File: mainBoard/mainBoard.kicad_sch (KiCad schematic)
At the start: 51 parts, among them J1 XT60PW-M, J10 XT30U_F, J11 XT30U_F, J2 XT60PW-M, J3 XT30PW-M, J4 XT30PW-M, J5 Barrel_Jack, J6 XT30U_F, J7 XT30U_F, J8 XT30U_F, J9 XT30U_F, Q1 FQD11P06TM, Q2 FQD11P06TM, U1 TPS54302, U2 TPS565208

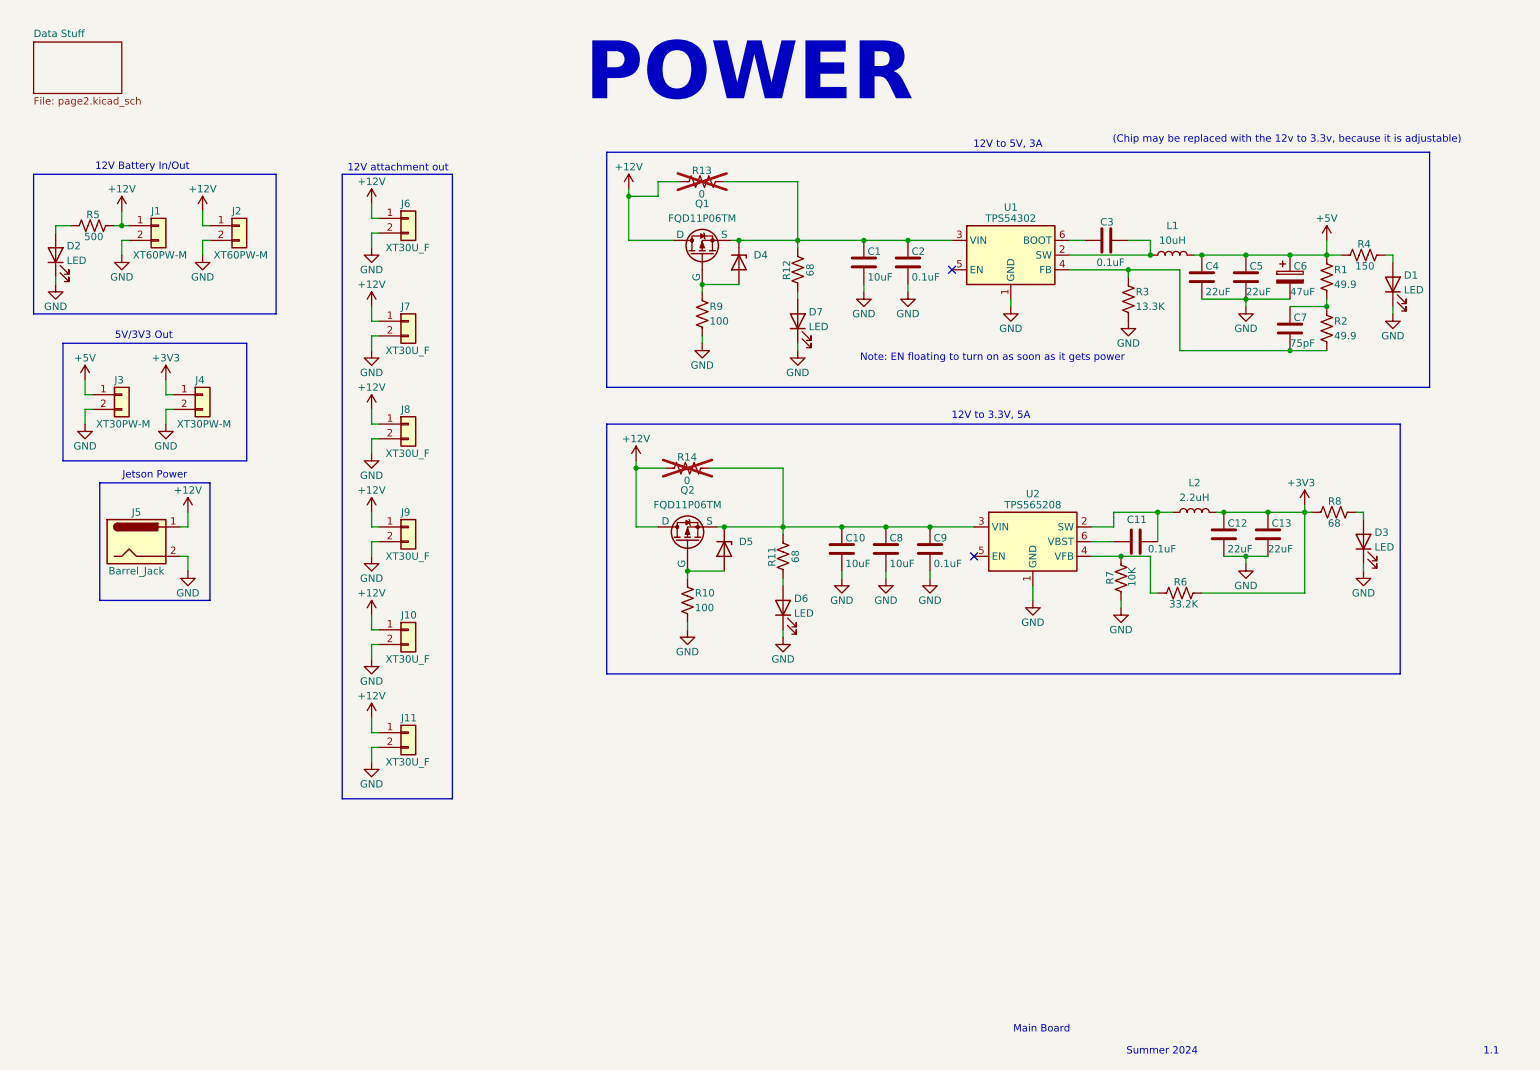
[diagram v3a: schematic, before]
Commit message: Added QWIIC Connectors for i2c, ethernet ports for attachment, updated XT style power connector counts, added i2c multiplexer
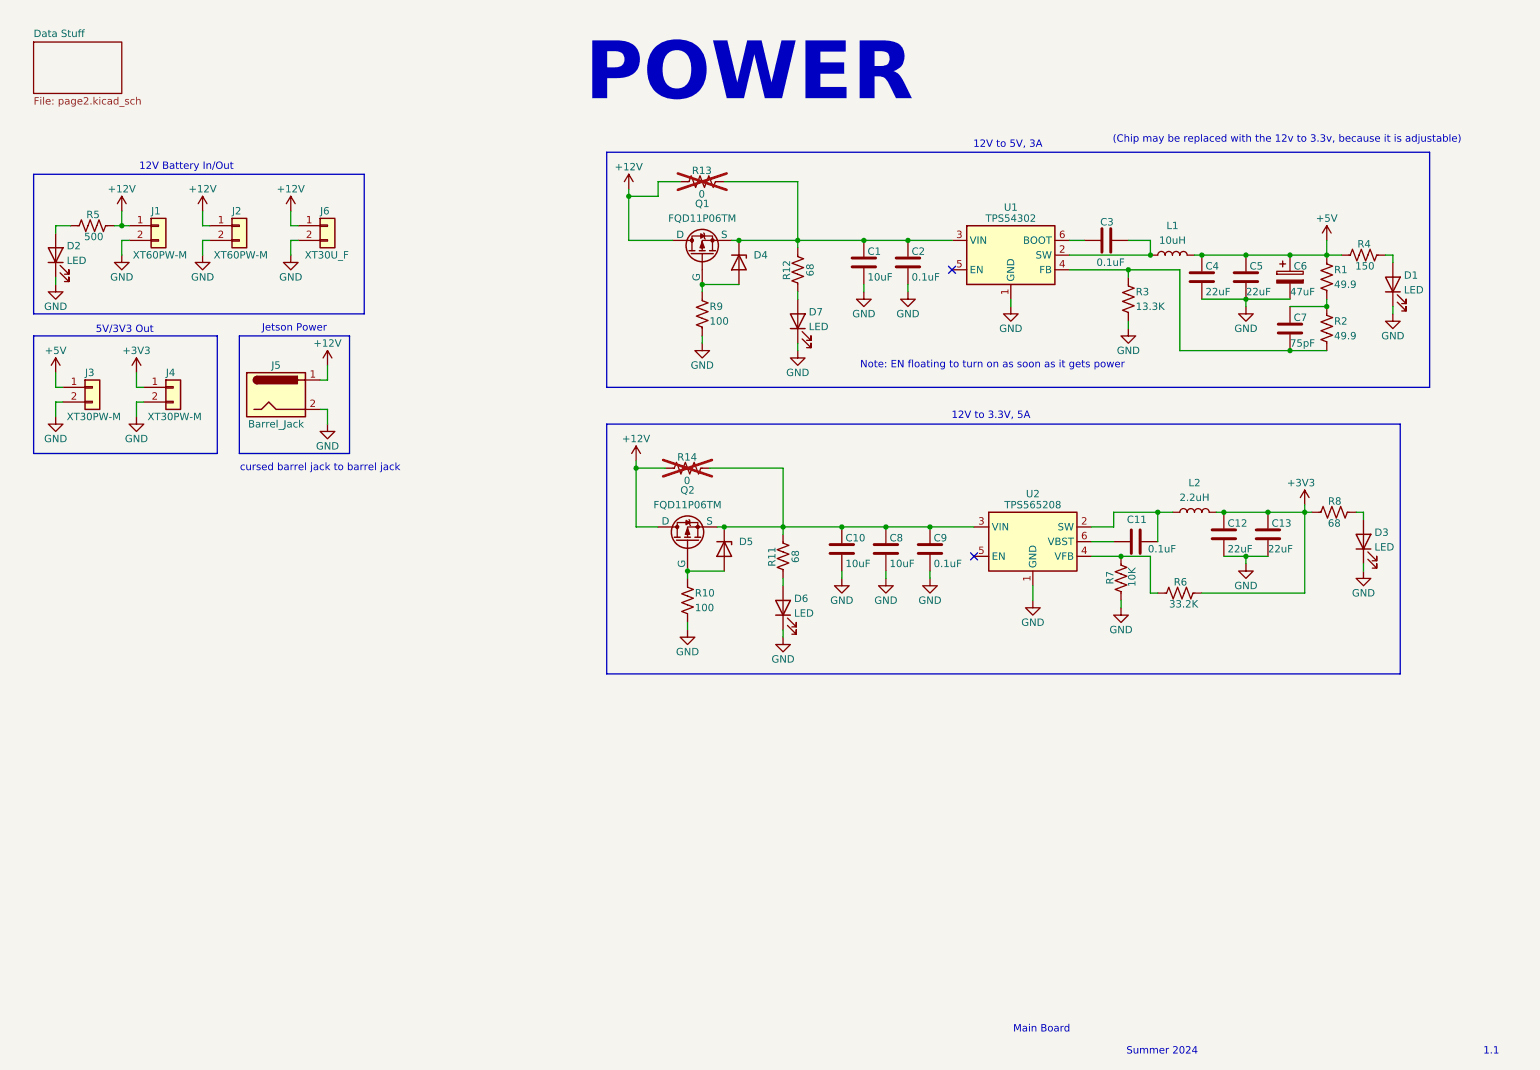
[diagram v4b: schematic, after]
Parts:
- removed J10, J11, J7, J8, J9: XT30U_F, Connector_AMASS:AMASS_XT30U-F_1x02_P5.0mm_Vertical, symbol Connector_Generic:Conn_01x02
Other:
- note added: "cursed barrel jack to barrel jack"
- note removed: "12V attachment out"
- moved on the sheet: J3, J4, J5, J6

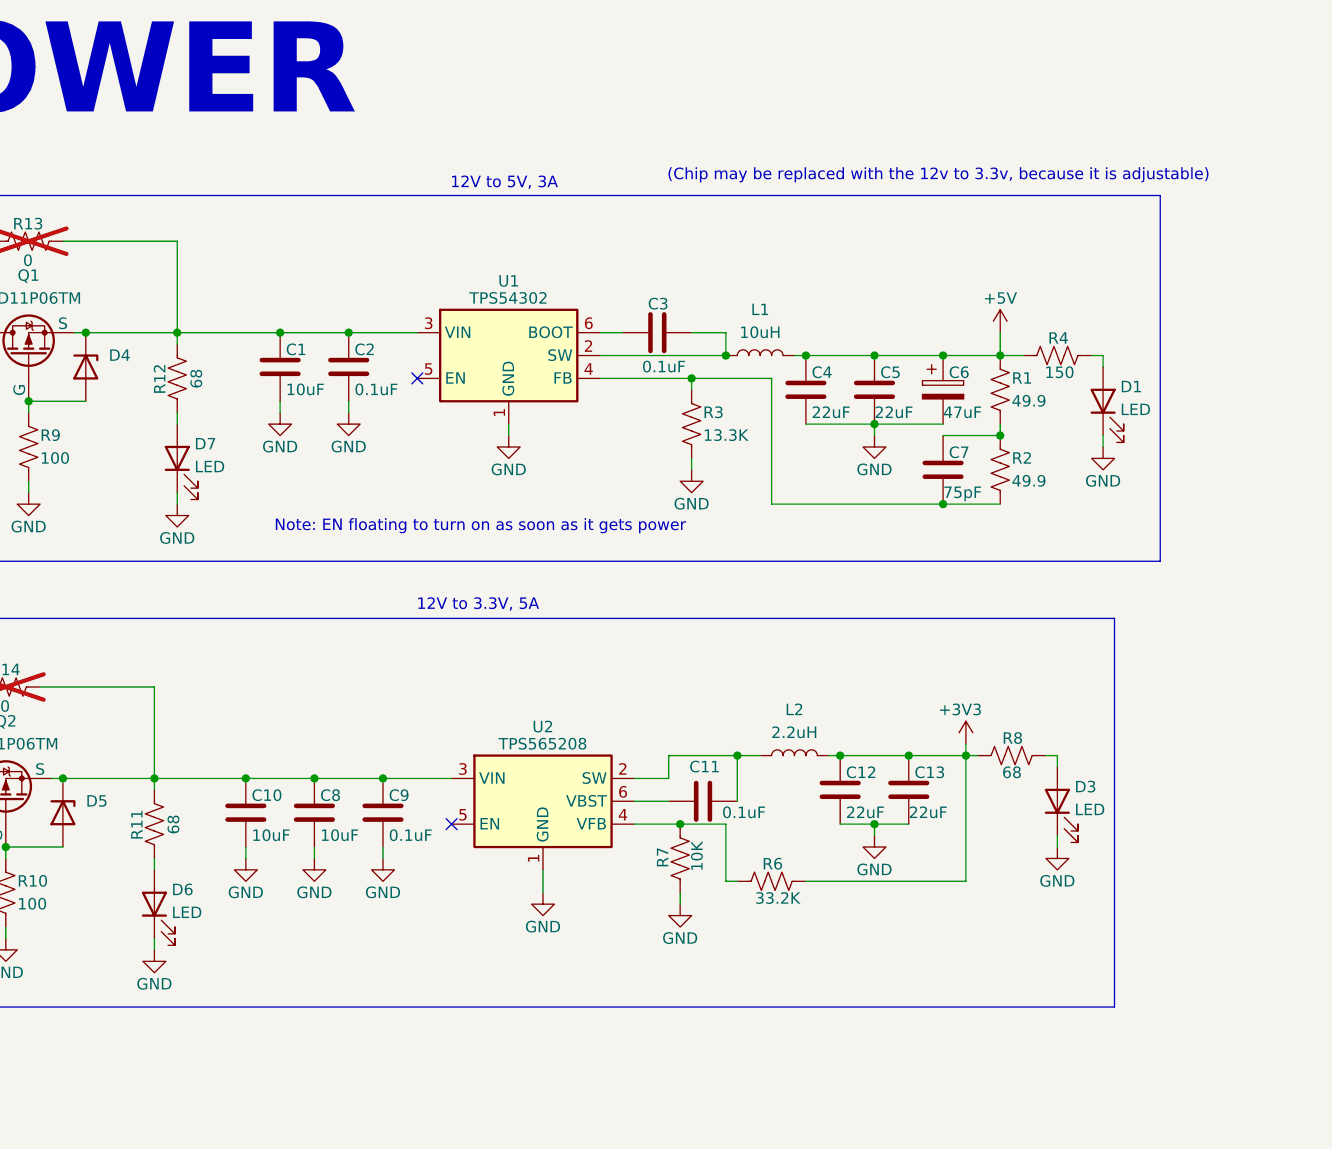
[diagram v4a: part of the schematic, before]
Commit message: Updated 12v to 5v chip to be the same as 3.3v, but with adjusted resistors
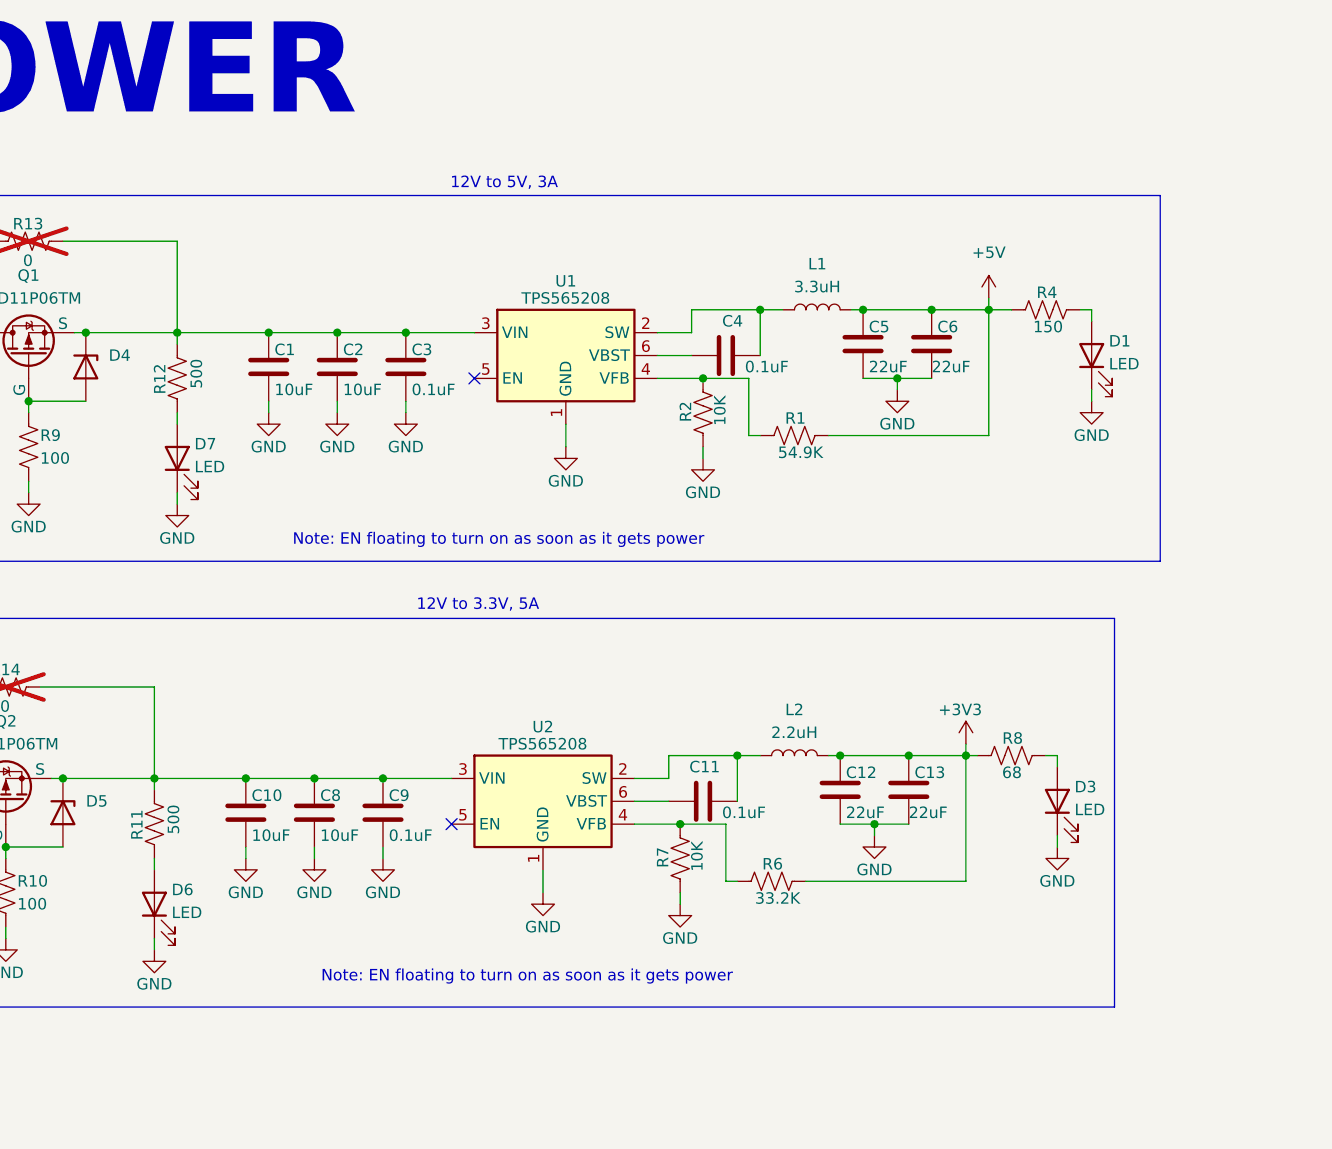
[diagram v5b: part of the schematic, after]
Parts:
- removed C6: 47uF, Capacitor_SMD:CP_Elec_6.3x5.4, symbol Device:C_Polarized
- removed C7: 75pF, Capacitor_SMD:C_0805_2012Metric_Pad1.18x1.45mm_HandSolder, symbol Device:C
- removed R3: 13.3K, Resistor_SMD:R_0805_2012Metric_Pad1.20x1.40mm_HandSolder, symbol Device:R_US
- removed U1: TPS54302, Package_TO_SOT_SMD:SOT-23-6, symbol Regulator_Switching:TPS54302
- added C6: 22uF, Capacitor_SMD:C_0805_2012Metric_Pad1.18x1.45mm_HandSolder, symbol Device:C
- added U1: TPS565208, Package_TO_SOT_SMD:SOT-23-6, symbol Regulator_Switching:TPS565208
- C2: value 0.1uF -> 10uF
- C4: value 22uF -> 0.1uF
- L1: value 10uH -> 3.3uH
- R1: value 49.9 -> 54.9K
- R11, R12: value 68 -> 500
- R2: value 49.9 -> 10K
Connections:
- net +5V: now also R1.2, C6.1; no longer C4.1, R1.1
- net GND: now also C3.2, R2.1, C6.2, U1.1 (GND); no longer C4.2
- net at C1.1, C2.1, D4.1 (K)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: now also C3.1, U1.3 (VIN)
- net at R2.2: now also R1.1, U1.4 (VFB)
- net at L1.1: now also C4.2, U1.2 (SW); no longer C3.2
- new net: C4.1, U1.6 (VBST)
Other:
- note removed: "(Chip may be replaced with the 12v to 3.3v, because it is adjustable)"
- moved on the sheet: D1, R4

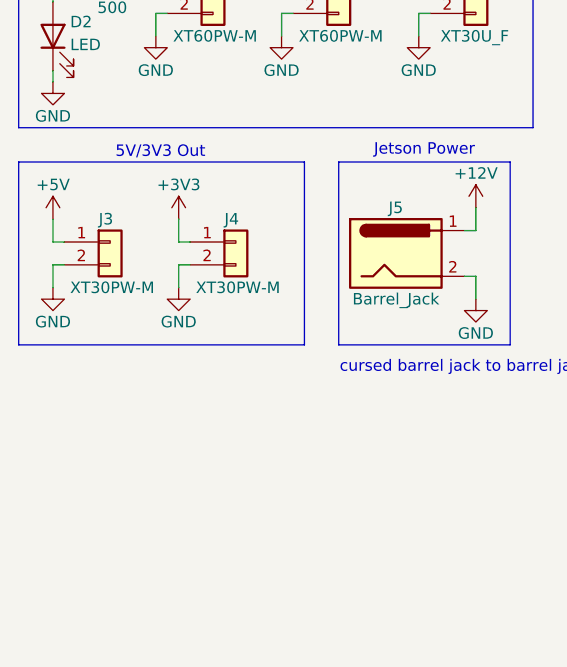
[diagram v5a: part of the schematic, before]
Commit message: Minor changes, renamed ethernet ports to attachment and adding warning
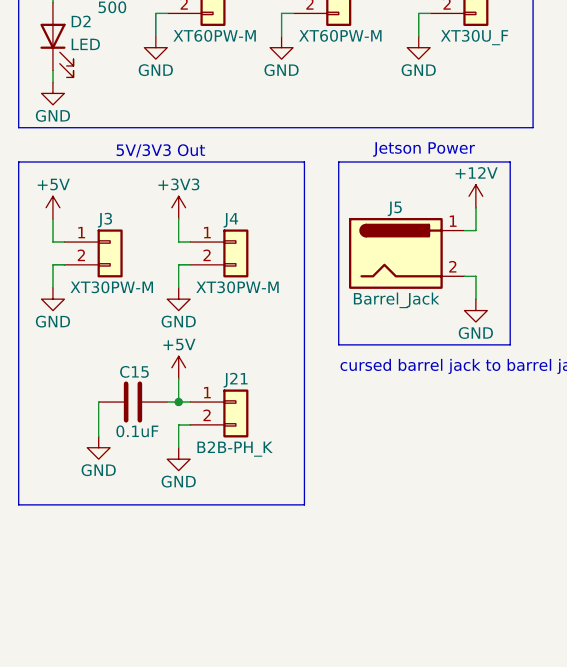
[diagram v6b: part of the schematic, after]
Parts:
- added C15: 0.1uF, Capacitor_SMD:C_0805_2012Metric_Pad1.18x1.45mm_HandSolder, symbol Device:C
- added J21: B2B-PH_K, Connector_JST:JST_PH_B2B-PH-K_1x02_P2.00mm_Vertical, symbol Connector_Generic:Conn_01x02
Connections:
- net +5V: now also C15.2, J21.1 (Pin_1)
- net GND: now also C15.1, J21.2 (Pin_2)

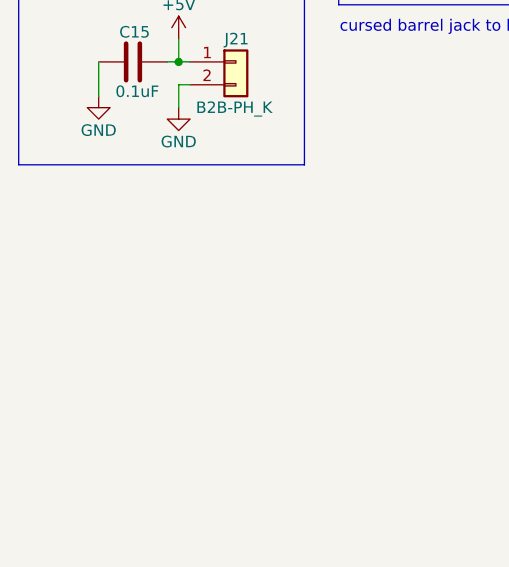
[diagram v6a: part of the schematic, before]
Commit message: Changed connector for jetson, adjusted layout, used vertical ethernet
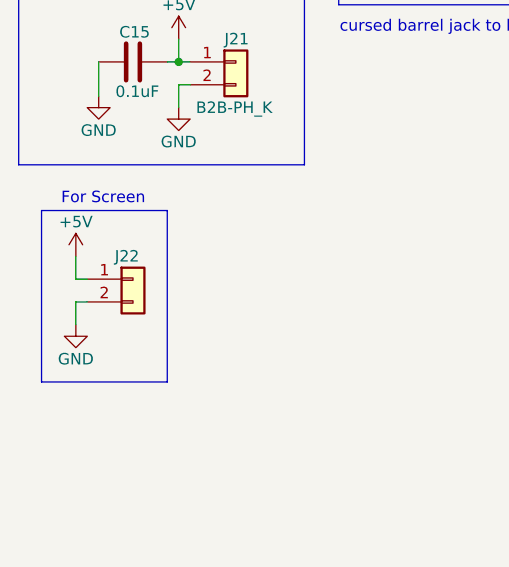
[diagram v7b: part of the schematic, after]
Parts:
- added J22: Conn_01x02, Connector_PinHeader_2.54mm:PinHeader_1x02_P2.54mm_Vertical, symbol Connector_Generic:Conn_01x02
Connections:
- net +5V: now also J22.1 (Pin_1)
- net GND: now also J22.2 (Pin_2)
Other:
- note added: "For Screen"

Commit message: did some rearangement, added 3d models that were missing
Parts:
- R13, R14: footprint Resistor_SMD:R_0805_2012Metric_Pad1.20x1.40mm_HandSolder -> Resistor_SMD:R_1210_3225Metric_Pad1.30x2.65mm_HandSolder
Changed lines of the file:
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@@
 			)
 		)
-		(property "Footprint" "Resistor_SMD:R_0805_2012Metric_Pad1.20x1.40mm_HandSolder"
+		(property "Footprint" "Resistor_SMD:R_1210_3225Metric_Pad1.30x2.65mm_HandSolder"
 			(at 133.096 44.196 90)
 			(effects
@@
 			)
 		)
-		(property "Footprint" "Resistor_SMD:R_0805_2012Metric_Pad1.20x1.40mm_HandSolder"
+		(property "Footprint" "Resistor_SMD:R_1210_3225Metric_Pad1.30x2.65mm_HandSolder"
 			(at 130.556 93.726 90)
 			(effects
